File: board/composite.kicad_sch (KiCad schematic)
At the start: 8 parts, among them U16 ATF1504AS-xAx44, Y3 25.175MHz, Y4 OSC2

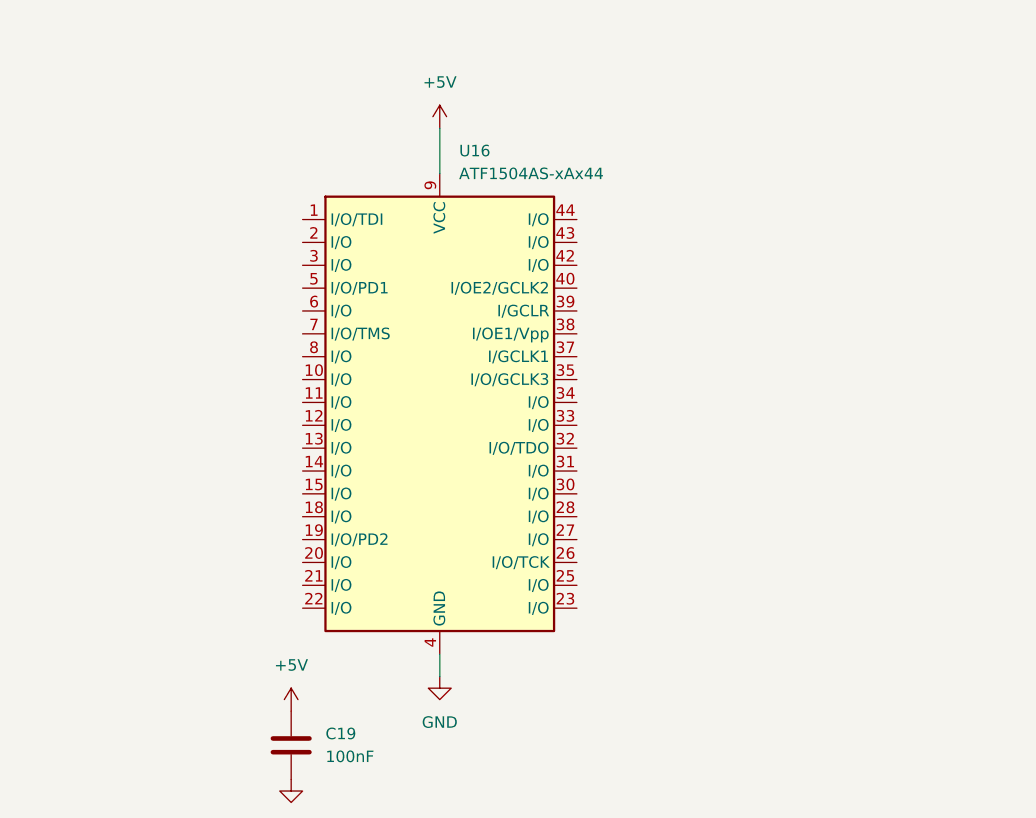
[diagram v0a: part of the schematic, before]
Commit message: capture TIMING; add PLCC44 ATF1504; a few fixes
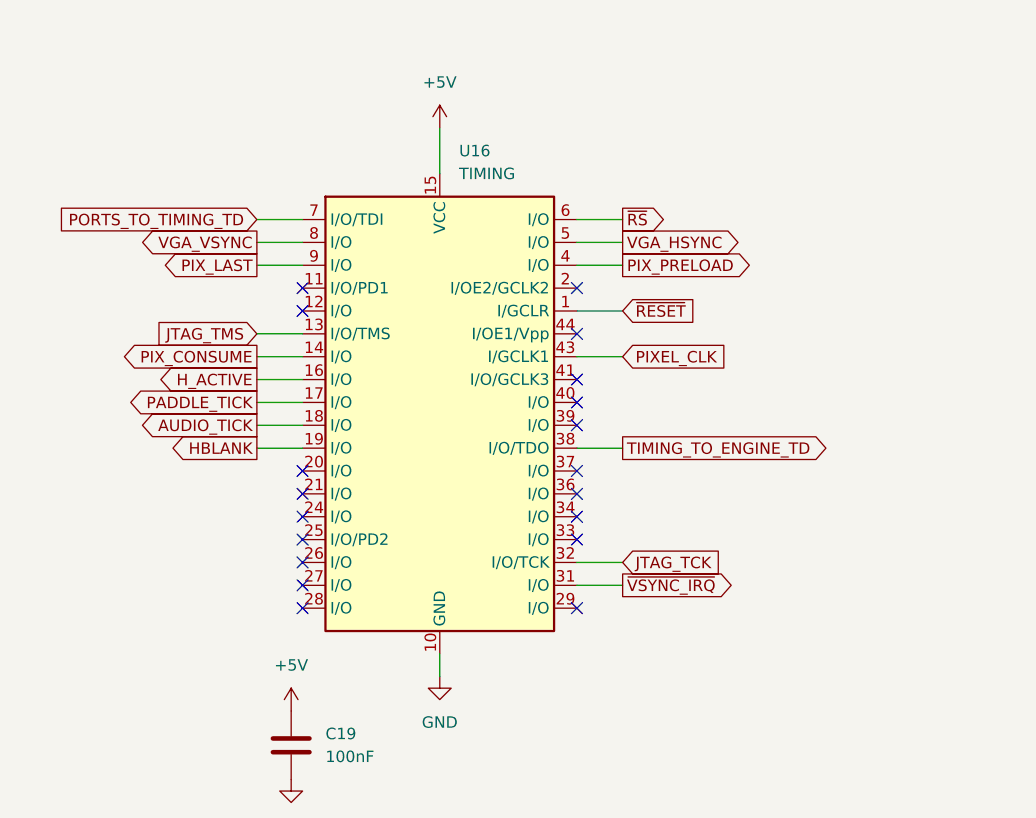
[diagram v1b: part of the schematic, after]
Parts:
- U16: value ATF1504AS-xAx44 -> TIMING; footprint Package_QFP:TQFP-44_10x10mm_P0.8mm -> Package_LCC:PLCC-44_THT-Socket; symbol CPLD_Microchip:ATF1504AS-xAx44 -> Griffin:ATF1504AS-xxJx44
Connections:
- net +5V: now also U16.15 (VCC), U16.23 (VCC), U16.3 (VCC), U16.35 (VCC); no longer U16.17 (VCC), U16.29 (VCC), U16.41 (VCC), U16.9 (VCC)
- net GND: now also U16.10 (GND), U16.22 (GND), U16.30 (GND), U16.42 (GND); no longer U16.16 (GND), U16.24 (GND), U16.36 (GND), U16.4 (GND)
- net PIXEL_CLK: now also U16.43 (I/GCLK1)
- net ~{RESET}: now reaches U16.1 (I/GCLR)
- net JTAG_TMS: now reaches U16.13 (I/O/TMS)
- net PIX_CONSUME: now reaches U16.14 (I/O)
- net AUDIO_TICK: now reaches U16.18 (I/O)
- net HBLANK: now reaches U16.19 (I/O)
- net ~{VSYNC_IRQ}: now reaches U16.31 (I/O)
- net JTAG_TCK: now reaches U16.32 (I/O/TCK)
- net TIMING_TO_ENGINE_TD: now reaches U16.38 (I/O/TDO)
- net VGA_HSYNC: now reaches U16.5 (I/O)
- net ~{RS}: now reaches U16.6 (I/O)
- net PORTS_TO_TIMING_TD: now reaches U16.7 (I/O/TDI)
- net VGA_VSYNC: now reaches U16.8 (I/O)
- new net H_ACTIVE: U16.16 (I/O)
- new net PADDLE_TICK: U16.17 (I/O)
- new net PIX_LAST: U16.9 (I/O)
- new net PIX_PRELOAD: U16.4 (I/O)
- no-connect marks 0 -> 19
